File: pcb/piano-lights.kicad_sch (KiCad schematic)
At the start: 36 parts, among them J1 FTDI RS232, J2 USB_B_Micro, J3 LED Strip, J4 AVR-ISP-6, J5 MIDI IN, J6 MIDI THRU, SW1 Button, SW2 Reset, U1 ATmega328P-P, U2 H11L1, U3 74AHC1G125, Y1 16MHz

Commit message: First pass at smaller PCB with MIDI coupler
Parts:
- added J7: MIDI Coupler Out, 00-Vendor_SDS-50J:CUI_SDS-50J, symbol 00-piano-lights:DIN-5_180degree_Shielded
- added J8: MIDI Coupler In, 00-Vendor_SDS-50J:CUI_SDS-50J, symbol 00-piano-lights:DIN-5_180degree_Shielded
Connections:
- new net MCOUP_DATA: J7.5, J8.5
- new net MCOUP_GND: J7.2, J8.2
- new net MCOUP_SH: J7.SH, J8.SH
- new net MCOUP_V: J7.4, J8.4
- no-connect marks 22 -> 26
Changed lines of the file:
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@@
   (no_connect (at 53.34 39.37))
   (no_connect (at 53.34 41.91))
+  (no_connect (at 215.9 139.954))
+  (no_connect (at 223.52 139.446))
   (no_connect (at 97.79 99.06))
+  (no_connect (at 238.76 139.446))
   (no_connect (at 130.81 63.5))
   (no_connect (at 130.81 101.6))
@@
   (no_connect (at 130.81 99.06))
   (no_connect (at 130.81 50.8))
+  (no_connect (at 200.914 139.954))
   (no_connect (at 200.66 29.21))
   (no_connect (at 200.66 39.37))
@@
     (stroke (width 0) (type default) (color 0 0 0 0))
   )
+  (wire (pts (xy 208.28 147.574) (xy 208.28 154.94))
+    (stroke (width 0) (type default) (color 0 0 0 0))
+  )
   (wire (pts (xy 165.1 100.33) (xy 165.1 101.6))
     (stroke (width 0) (type default) (color 0 0 0 0))
@@
     (stroke (width 0) (type default) (color 0 0 0 0))
   )
+  (wire (pts (xy 220.98 141.986) (xy 223.52 141.986))
+    (stroke (width 0) (type default) (color 0 0 0 0))
+  )
   (wire (pts (xy 114.3 34.29) (xy 116.84 34.29))
     (stroke (width 0) (type default) (color 0 0 0 0))
@@
     (stroke (width 0) (type default) (color 0 0 0 0))
   )
+  (wire (pts (xy 246.38 141.986) (xy 238.76 141.986))
+    (stroke (width 0) (type default) (color 0 0 0 0))
+  )
   (polyline (pts (xy 191.77 78.74) (xy 228.6 78.74))
     (stroke (width 0) (type default) (color 0 0 0 0))
@@
     (stroke (width 0) (type default) (color 0 0 0 0))
   )
+  (wire (pts (xy 208.28 127) (xy 231.14 127))
+    (stroke (width 0) (type default) (color 0 0 0 0))
+  )
   (wire (pts (xy 90.805 24.13) (xy 90.805 25.4))
     (stroke (width 0) (type default) (color 0 0 0 0))
@@
     (stroke (width 0) (type default) (color 0 0 0 0))
   )
+  (wire (pts (xy 246.38 152.4) (xy 246.38 141.986))
+    (stroke (width 0) (type default) (color 0 0 0 0))
+  )
   (wire (pts (xy 90.17 67.31) (xy 90.17 66.04))
     (stroke (width 0) (type default) (color 0 0 0 0))
@@
     (stroke (width 0) (type default) (color 0 0 0 0))
   )
+  (wire (pts (xy 231.14 127) (xy 231.14 130.556))
+    (stroke (width 0) (type default) (color 0 0 0 0))
+  )
   (wire (pts (xy 125.73 136.525) (xy 125.73 135.89))
     (stroke (width 0) (type default) (color 0 0 0 0))
@@
     (stroke (width 0) (type default) (color 0 0 0 0))
   )
+  (wire (pts (xy 200.66 142.494) (xy 198.12 142.494))
+    (stroke (width 0) (type default) (color 0 0 0 0))
+  )
+  (wire (pts (xy 198.12 149.86) (xy 220.98 149.86))
+    (stroke (width 0) (type default) (color 0 0 0 0))
+  )
   (polyline (pts (xy 100.33 125.73) (xy 100.33 165.1))
     (stroke (width 0) (type default) (color 0 0 0 0))
@@
     (stroke (width 0) (type default) (color 0 0 0 0))
   )
+  (wire (pts (xy 198.12 142.494) (xy 198.12 149.86))
+    (stroke (width 0) (type default) (color 0 0 0 0))
+  )
   (wire (pts (xy 53.975 105.41) (xy 53.975 106.68))
     (stroke (width 0) (type default) (color 0 0 0 0))
@@
     (stroke (width 0) (type default) (color 0 0 0 0))
   )
+  (wire (pts (xy 220.98 149.86) (xy 220.98 141.986))
+    (stroke (width 0) (type default) (color 0 0 0 0))
+  )
   (wire (pts (xy 213.36 110.49) (xy 213.36 109.22))
     (stroke (width 0) (type default) (color 0 0 0 0))
@@
     (stroke (width 0) (type default) (color 0 0 0 0))
   )
+  (wire (pts (xy 208.28 131.064) (xy 208.28 127))
+    (stroke (width 0) (type default) (color 0 0 0 0))
+  )
   (wire (pts (xy 95.25 101.6) (xy 95.25 149.86))
     (stroke (width 0) (type default) (color 0 0 0 0))
@@
     (stroke (width 0) (type default) (color 0 0 0 0))
   )
+  (wire (pts (xy 208.28 154.94) (xy 231.14 154.94))
+    (stroke (width 0) (type default) (color 0 0 0 0))
+  )
   (wire (pts (xy 42.545 169.545) (xy 48.26 169.545))
     (stroke (width 0) (type default) (color 0 0 0 0))
@@
     (stroke (width 0) (type default) (color 0 0 0 0))
   )
+  (wire (pts (xy 218.44 142.494) (xy 218.44 152.4))
+    (stroke (width 0) (type default) (color 0 0 0 0))
+  )
   (wire (pts (xy 80.01 59.69) (xy 80.01 60.96))
     (stroke (width 0) (type default) (color 0 0 0 0))
@@
     (stroke (width 0) (type default) (color 0 0 0 0))
   )
+  (wire (pts (xy 215.9 142.494) (xy 218.44 142.494))
+    (stroke (width 0) (type default) (color 0 0 0 0))
+  )
   (wire (pts (xy 42.545 167.64) (xy 42.545 169.545))
     (stroke (width 0) (type default) (color 0 0 0 0))
@@
     (stroke (width 0) (type default) (color 0 0 0 0))
   )
+  (wire (pts (xy 231.14 154.94) (xy 231.14 147.066))
+    (stroke (width 0) (type default) (color 0 0 0 0))
+  )
   (polyline (pts (xy 35.56 200.66) (xy 35.56 184.15))
     (stroke (width 0) (type default) (color 0 0 0 0))
@@
   )
   (wire (pts (xy 156.21 104.14) (xy 156.21 102.87))
+    (stroke (width 0) (type default) (color 0 0 0 0))
+  )
+  (wire (pts (xy 218.44 152.4) (xy 246.38 152.4))
     (stroke (width 0) (type default) (color 0 0 0 0))
   )
@@
     (effects (font (size 1.27 1.27)) (justify left bottom))
   )
+  (label "MCOUP_DATA" (at 232.41 152.4 0)
+    (effects (font (size 1.27 1.27)) (justify left bottom))
+  )
   (label "MTHRU_DATA_R" (at 127 149.86 0)
     (effects (font (size 0.635 0.635)) (justify left bottom))
   )
+  (label "MCOUP_SH" (at 215.9 127 0)
+    (effects (font (size 1.27 1.27)) (justify left bottom))
+  )
   (label "MIN_DATA" (at 41.91 106.68 0)
     (effects (font (size 1.27 1.27)) (justify left bottom))
@@
   )
   (label "~{RESET}" (at 132.715 78.74 0)
+    (effects (font (size 1.27 1.27)) (justify left bottom))
+  )
+  (label "MCOUP_GND" (at 214.63 154.94 0)
+    (effects (font (size 1.27 1.27)) (justify left bottom))
+  )
+  (label "MCOUP_V" (at 198.12 149.86 0)
     (effects (font (size 1.27 1.27)) (justify left bottom))
   )
@@
       (effects (font (size 1.27 1.27)) hide)
     )
+    (property "Mrf" "" (id 4) (at 163.83 139.7 0)
+      (effects (font (size 1.27 1.27)) hide)
+    )
+    (property "Part No" "" (id 5) (at 163.83 139.7 0)
+      (effects (font (size 1.27 1.27)) hide)
+    )
+    (property "Vendor" "" (id 6) (at 163.83 139.7 0)
+      (effects (font (size 1.27 1.27)) hide)
+    )
     (pin "1")
     (pin "2")
@@
     (pin "SH")
   )
+  (symbol (lib_id "00-piano-lights:DIN-5_180degree_Shielded") (at 208.28 139.954 0) (mirror x) (unit 1)
+    (in_bom yes) (on_board yes)
+    (property "Reference" "J8" (id 0) (at 209.55 131.064 0)
+      (effects (font (size 1.27 1.27)) (justify left))
+    )
+    (property "Value" "MIDI Coupler In" (id 1) (at 209.55 133.604 0)
+      (effects (font (size 1.27 1.27)) (justify left))
+    )
+    (property "Footprint" "00-Vendor_SDS-50J:CUI_SDS-50J" (id 2) (at 208.28 139.954 0)
+      (effects (font (size 1.27 1.27)) hide)
+    )
+    (property "Datasheet" "https://www.cuidevices.com/product/resource/sds-j.pdf" (id 3) (at 208.28 139.954 0)
+      (effects (font (size 1.27 1.27)) hide)
+    )
+    (property "Mrf" "CUI" (id 4) (at 208.28 139.954 0)
+      (effects (font (size 1.27 1.27)) hide)
+    )
+    (property "Part No" "SDS-50J" (id 5) (at 208.28 139.954 0)
+      (effects (font (size 1.27 1.27)) hide)
+    )
+    (property "Vendor" "https://www.digikey.com/en/products/detail/cui-devices/SDS-50J/97033" (id 6) (at 208.28 139.954 0)
+      (effects (font (size 1.27 1.27)) hide)
+    )
+    (pin "1")
+    (pin "2")
+    (pin "3")
+    (pin "4")
+    (pin "5")
+    (pin "SH")
+  )
   (symbol (lib_id "Device:LED") (at 151.13 104.14 0) (mirror x) (unit 1)
     (in_bom yes) (on_board yes)
@@
     (pin "1")
   )
+  (symbol (lib_id "00-piano-lights:DIN-5_180degree_Shielded") (at 231.14 139.446 0) (mirror x) (unit 1)
+    (in_bom yes) (on_board yes)
+    (property "Reference" "J7" (id 0) (at 232.41 130.556 0)
+      (effects (font (size 1.27 1.27)) (justify left))
+    )
+    (property "Value" "MIDI Coupler Out" (id 1) (at 232.41 133.096 0)
+      (effects (font (size 1.27 1.27)) (justify left))
+    )
+    (property "Footprint" "00-Vendor_SDS-50J:CUI_SDS-50J" (id 2) (at 231.14 139.446 0)
+      (effects (font (size 1.27 1.27)) hide)
+    )
+    (property "Datasheet" "http://www.mouser.com/ds/2/18/40_c091_abd_e-75918.pdf" (id 3) (at 231.14 139.446 0)
+      (effects (font (size 1.27 1.27)) hide)
+    )
+    (property "Mrf" "" (id 4) (at 231.14 139.446 0)
+      (effects (font (size 1.27 1.27)) hide)
+    )
+    (property "Part No" "" (id 5) (at 231.14 139.446 0)
+      (effects (font (size 1.27 1.27)) hide)
+    )
+    (property "Vendor" "" (id 6) (at 231.14 139.446 0)
+      (effects (font (size 1.27 1.27)) hide)
+    )
+    (pin "1")
+    (pin "2")
+    (pin "3")
+    (pin "4")
+    (pin "5")
+    (pin "SH")
+  )
   (symbol (lib_id "power:+5V") (at 213.36 85.09 0) (mirror y) (unit 1)
     (in_bom yes) (on_board yes)
@@
       (reference "J6") (unit 1) (value "MIDI THRU") (footprint "00-Vendor_SDS-50J:CUI_SDS-50J")
     )
+    (path "/f9866f8b-3936-4706-bae6-722d71235ee8"
+      (reference "J7") (unit 1) (value "MIDI Coupler Out") (footprint "00-Vendor_SDS-50J:CUI_SDS-50J")
+    )
+    (path "/c47e7649-31b9-489c-93da-965a4a52c822"
+      (reference "J8") (unit 1) (value "MIDI Coupler In") (footprint "00-Vendor_SDS-50J:CUI_SDS-50J")
+    )
     (path "/f3058dab-f2e9-49c6-8907-75a98c2494ef"

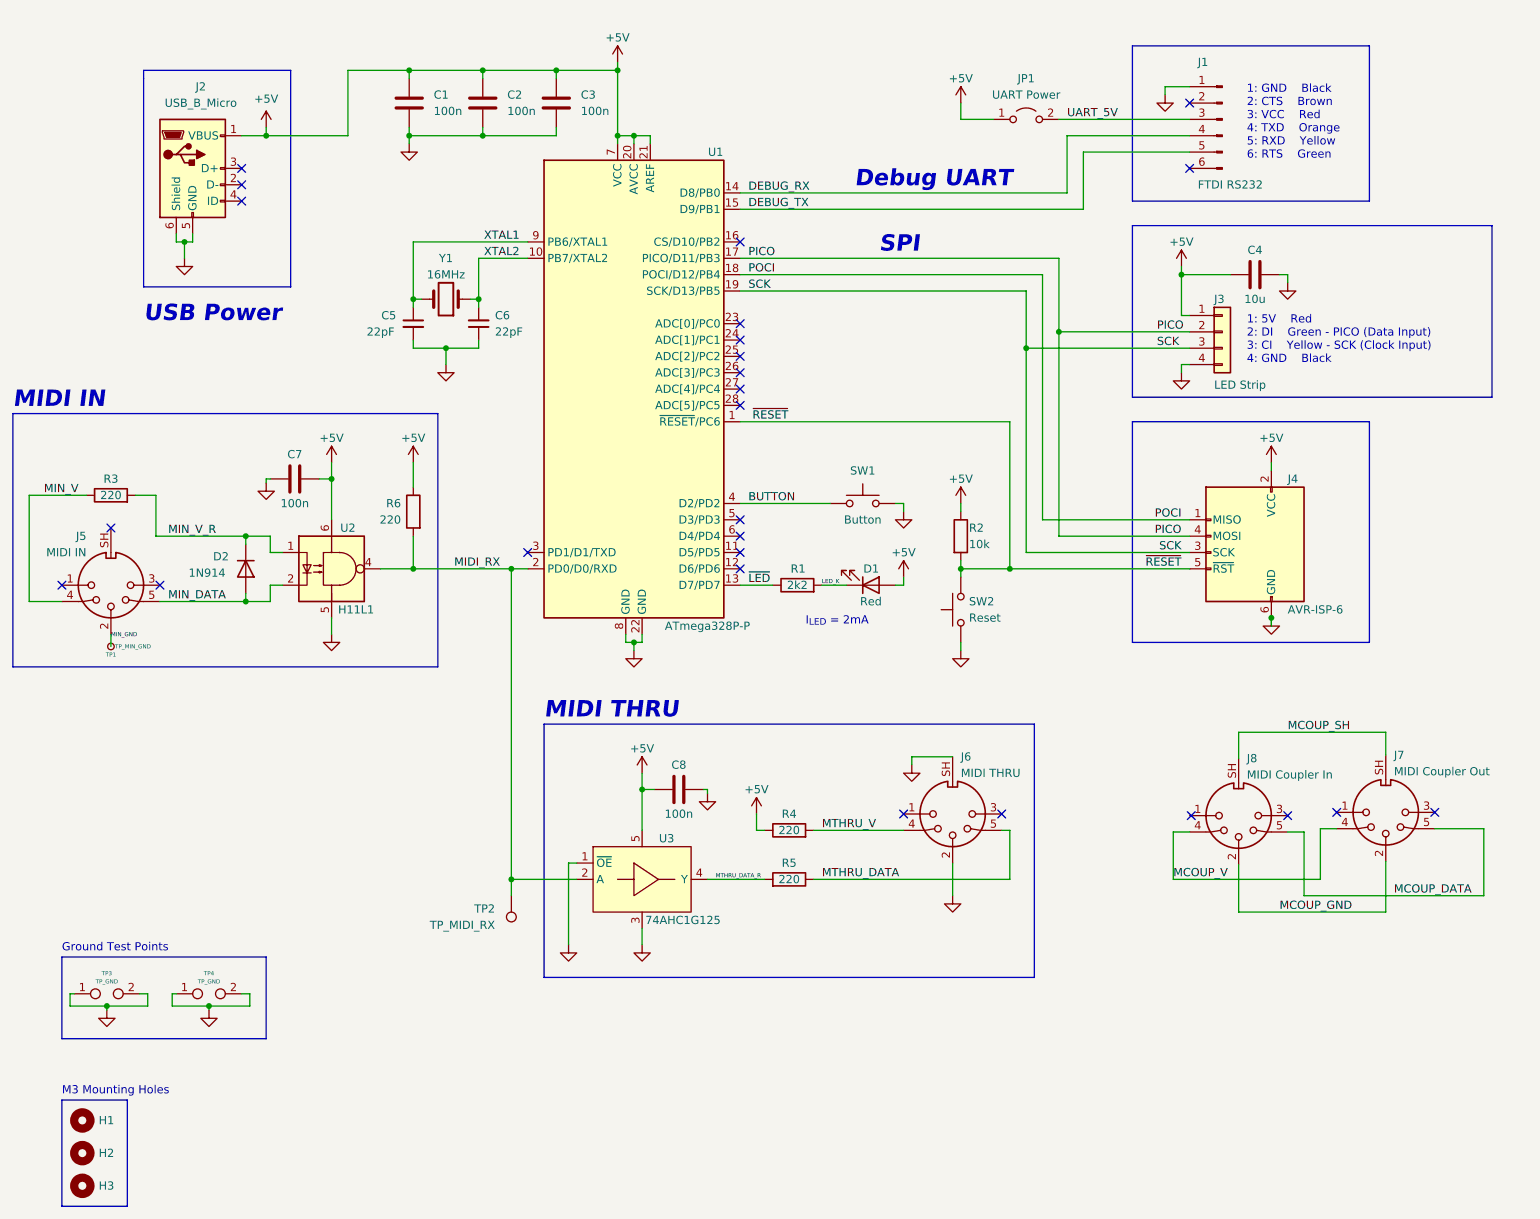
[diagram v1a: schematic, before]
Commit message: Fix up schematic, update to SMD CPU, and start laying out board
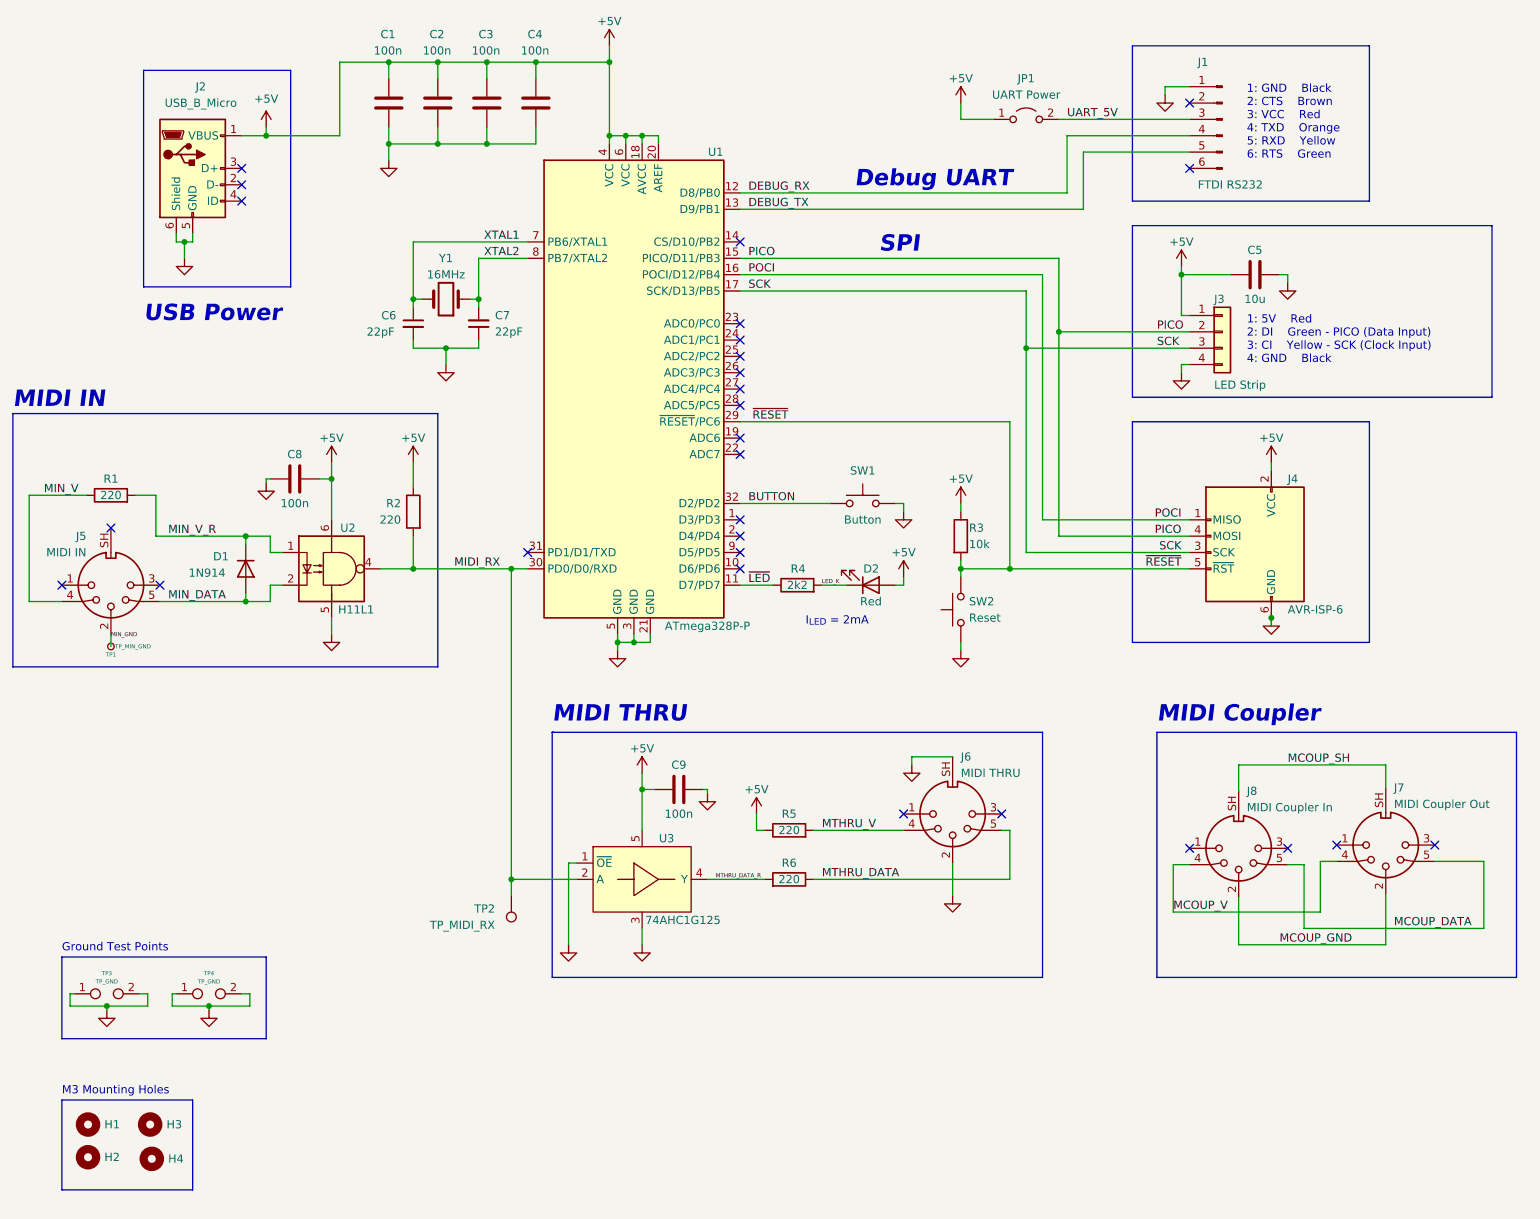
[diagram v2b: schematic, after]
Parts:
- added C1: 100n, Capacitor_SMD:C_0805_2012Metric_Pad1.18x1.45mm_HandSolder, symbol Device:C
- added H4: MountingHole, MountingHole:MountingHole_3.2mm_M3, symbol Mechanical:MountingHole
- J3: footprint Connector_Wire:SolderWire-0.25sqmm_1x04_P4.5mm_D0.65mm_OD2mm_Relief -> Connector_Wire:SolderWire-0.15sqmm_1x04_P4mm_D0.5mm_OD1.5mm_Relief
- U1: footprint Package_DIP:DIP-28_W7.62mm -> Package_QFP:TQFP-32_7x7mm_P0.8mm; symbol 00-piano-lights:ATmega328P-P -> 00-piano-lights:ATmega328-A
- renumbered C1 to C2, C2 to C3, C3 to C4, C4 to C5, C5 to C6, C6 to C7, C7 to C8, C8 to C9, D2 to D1, D1 to D2, R3 to R1, R6 to R2, R2 to R3, R1 to R4, R4 to R5, R5 to R6
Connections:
- net +5V: now also U1.18 (AVCC), U1.4 (VCC), U1.6 (VCC), C1.1; no longer U1.21 (AREF), U1.7 (VCC)
- net BUTTON: now also U1.32 (D2/PD2); no longer U1.4 (D2/PD2)
- net DEBUG_RX: now also U1.12 (D8/PB0); no longer U1.14 (D8/PB0)
- net DEBUG_TX: now also U1.13 (D9/PB1); no longer U1.15 (D9/PB1)
- net GND: now also U1.21 (GND), U1.3 (GND), U1.5 (GND), C1.2; no longer U1.22 (GND), U1.8 (GND)
- net MIDI_RX: now also U1.30 (PD0/D0/RXD); no longer U1.2 (PD0/D0/RXD)
- net PICO: now also U1.15 (PICO/D11/PB3); no longer U1.17 (PICO/D11/PB3)
- net POCI: now also U1.16 (POCI/D12/PB4); no longer U1.18 (POCI/D12/PB4)
- net SCK: now also U1.17 (SCK/D13/PB5); no longer U1.19 (SCK/D13/PB5)
- net XTAL1: now also U1.7 (PB6/XTAL1); no longer U1.9 (PB6/XTAL1)
- net XTAL2: now also U1.8 (PB7/XTAL2); no longer U1.10 (PB7/XTAL2)
- net ~{LED}: now also U1.11 (D7/PD7); no longer U1.13 (D7/PD7)
- net ~{RESET}: now also U1.29 (~{RESET}/PC6); no longer U1.1 (~{RESET}/PC6)
- no-connect marks 26 -> 28
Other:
- note added: "MIDI Coupler"
- moved on the sheet: C2, C3, C4, H1, H2, H3, J7, J8

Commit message: More PCB routing
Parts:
- removed SW1: Button, Button_Switch_THT:SW_PUSH_6mm_H5mm, symbol Switch:SW_Push
- removed TP1: TP_MIN_GND, TestPoint:TestPoint_Pad_2.0x2.0mm, symbol Connector:TestPoint_Small
- removed TP2: TP_MIDI_RX, TestPoint:TestPoint_Pad_2.0x2.0mm, symbol Connector:TestPoint
- removed TP3, TP4: TP_GND, Connector_PinHeader_2.54mm:PinHeader_1x02_P2.54mm_Vertical, symbol Connector:TestPoint_2Pole
- C1, C2, C3, C4, C6, C7, C8, C9: footprint Capacitor_SMD:C_0805_2012Metric_Pad1.18x1.45mm_HandSolder -> Capacitor_SMD:C_0603_1608Metric_Pad1.08x0.95mm_HandSolder
- R1, R2, R3, R4, R5, R6: footprint Resistor_SMD:R_0805_2012Metric_Pad1.20x1.40mm_HandSolder -> Resistor_SMD:R_0603_1608Metric_Pad0.98x0.95mm_HandSolder
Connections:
- net BUTTON: no longer names the net of U1.32 (D2/PD2)
- net MIN_GND: no longer names the net of J5.2
- no-connect marks 28 -> 30
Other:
- note removed: "Ground Test Points"
